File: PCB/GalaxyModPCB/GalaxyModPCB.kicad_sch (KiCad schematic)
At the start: 55 parts, among them J1 Power Header, J2 Boot mode, J3 LED RGBW Connector, J4 JTAG, J5 USB to UART, J6 Motor Connector, J7 Projector Connector, Q1 BC817-40-7-F, Q2 BC817-40-7-F, Q3 BC817-40-7-F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

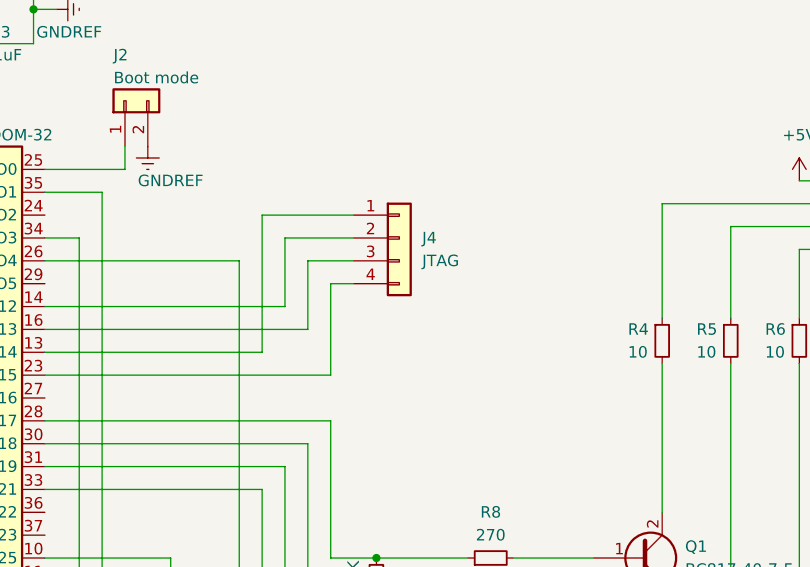
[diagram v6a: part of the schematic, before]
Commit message: added gnd to jtag connector -> routing up next
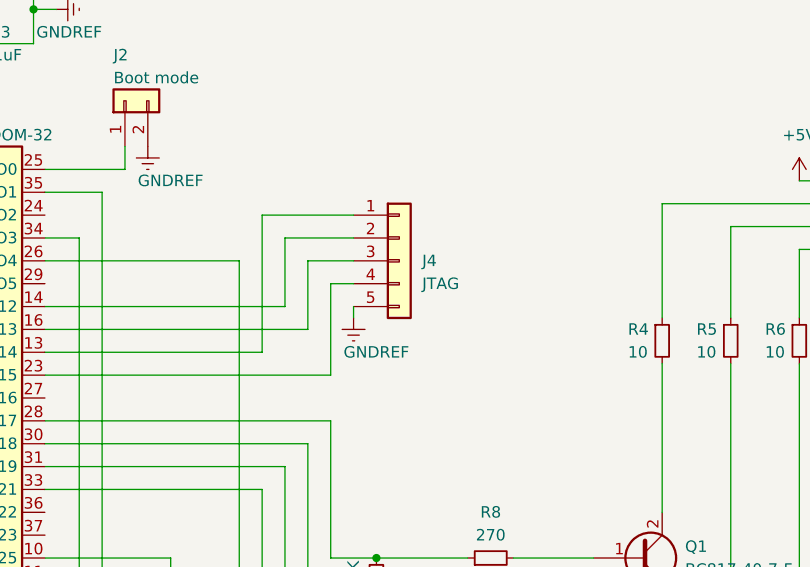
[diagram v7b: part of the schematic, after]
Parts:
- J4: symbol Connector_Generic:Conn_01x04 -> Connector_Generic:Conn_01x05
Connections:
- net GNDREF: now also J4.5 (Pin_5)
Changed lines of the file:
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@@
+    (stroke (width 0) (type default))
+  )
+  (wire (pts (xy 181.61 78.74) (xy 181.61 80.01))
     (stroke (width 0) (type default))
   )
@@
     )
   )
-  (symbol (lib_id "Connector_Generic:Conn_01x04") (at 186.69 71.12 0) (unit 1)
-    (in_bom yes) (on_board yes) (dnp no) (fields_autoplaced)
-    (property "Reference" "J4" (at 189.23 71.1199 0)
-      (effects (font (size 1.27 1.27)) (justify left))
-    )
-    (property "Value" "JTAG" (at 189.23 73.6599 0)
-      (effects (font (size 1.27 1.27)) (justify left))
-    )
-    (property "Footprint" "Jumper:SolderJumper-3_P1.3mm_Open_Pad1.0x1.5mm_NumberLabels" (at 186.69 71.12 0)
-      (effects (font (size 1.27 1.27)) hide)
-    )
-    (property "Datasheet" "~" (at 186.69 71.12 0)
+  (symbol (lib_id "Connector_Generic:Conn_01x05") (at 186.69 73.66 0) (unit 1)
+    (in_bom yes) (on_board yes) (dnp no) (fields_autoplaced)
+    (property "Reference" "J4" (at 189.23 73.6599 0)
+      (effects (font (size 1.27 1.27)) (justify left))
+    )
+    (property "Value" "JTAG" (at 189.23 76.1999 0)
+      (effects (font (size 1.27 1.27)) (justify left))
+    )
+    (property "Footprint" "Jumper:SolderJumper-3_P1.3mm_Open_Pad1.0x1.5mm_NumberLabels" (at 186.69 73.66 0)
+      (effects (font (size 1.27 1.27)) hide)
+    )
+    (property "Datasheet" "~" (at 186.69 73.66 0)
       (effects (font (size 1.27 1.27)) hide)
     )
@@
     (pin "3")
     (pin "4")
+    (pin "5")
     (instances
       (project "GalaxyModPCB"
@@
         )
       )
+    )
+  )
+  (symbol (lib_id "power:GNDREF") (at 181.61 80.01 0) (unit 1)
+    (in_bom yes) (on_board yes) (dnp no)
+    (property "Reference" "#PWR030" (at 181.61 86.36 0)
+      (effects (font (size 1.27 1.27)) hide)
+    )
+    (property "Value" "GNDREF" (at 184.15 83.82 0)
+      (effects (font (size 1.27 1.27)))
+    )
+    (property "Footprint" "" (at 181.61 80.01 0)
+      (effects (font (size 1.27 1.27)) hide)
+    )
+    (property "Datasheet" "" (at 181.61 80.01 0)
+      (effects (font (size 1.27 1.27)) hide)
+    )
+    (pin "1")
+    (instances
+      (project "GalaxyModPCB"
+        (path "/74bbbacb-c982-4615-b32e-142a16798fae"
+          (reference "#PWR030") (unit 1)
+        )
+      )

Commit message: Updated Kicad and LED
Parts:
- D2: footprint LED_SMD:LED_0805_2012Metric -> LED_SMD:LED_0201_0603Metric_Pad0.64x0.40mm_HandSolder
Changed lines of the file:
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@@
       (effects (font (size 1.27 1.27)) (justify right))
     )
-    (property "Footprint" "LED_SMD:LED_0805_2012Metric" (at 76.2 52.07 0)
+    (property "Footprint" "LED_SMD:LED_0201_0603Metric_Pad0.64x0.40mm_HandSolder" (at 76.2 52.07 0)
       (effects (font (size 1.27 1.27)) hide)
     )
-    (property "Datasheet" "~" (at 76.2 52.07 0)
+    (property "Datasheet" "https://www.digikey.co.uk/en/products/detail/liteon/LTST-C190KRKT/386817" (at 76.2 52.07 0)
       (effects (font (size 1.27 1.27)) hide)
     )
